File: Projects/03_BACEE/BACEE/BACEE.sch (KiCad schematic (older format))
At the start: 13 parts, among them U1 DS1337_MLv1, U2 24LC1025, U3 24LC1025, U4 ATmega328P-AU, Y1 Crystal 32MHz, Y2 Crystal 16MHz

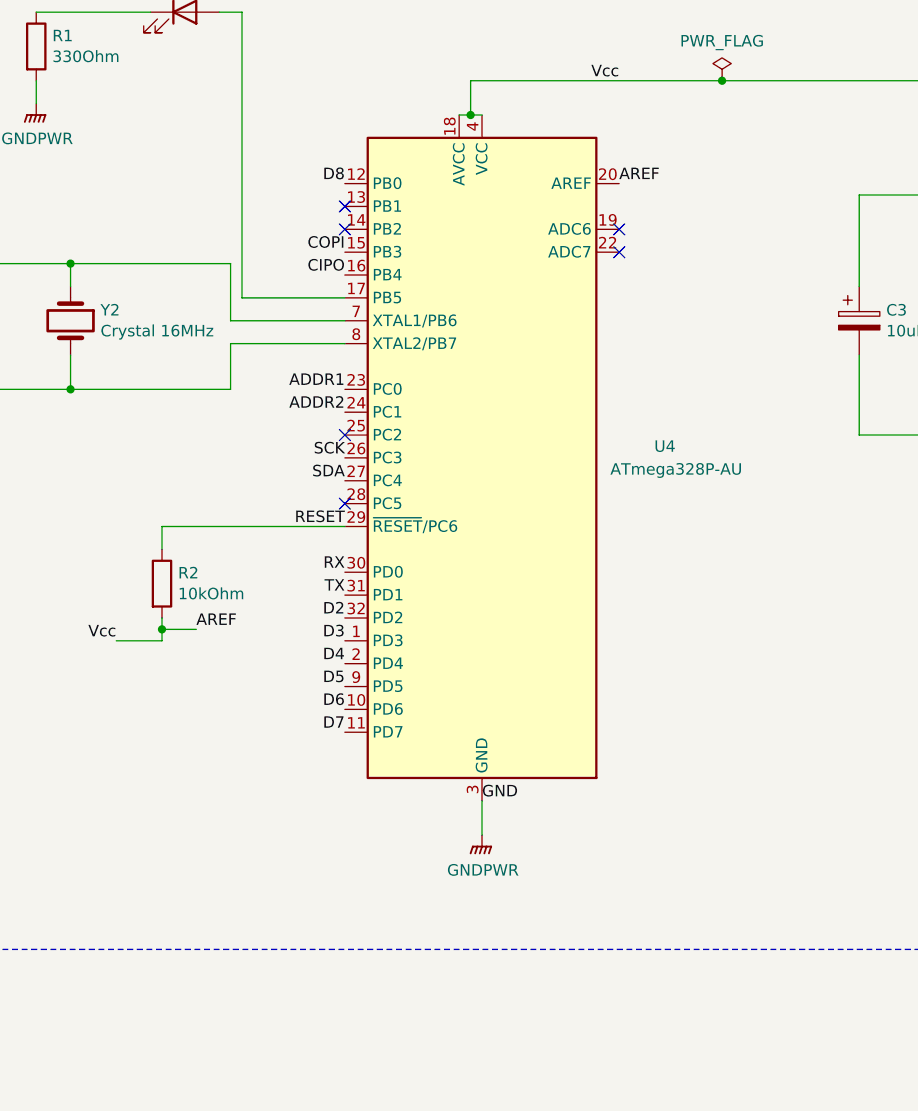
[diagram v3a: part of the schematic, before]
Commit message: Project 3: Edit schematic by changing AREF to Vcc
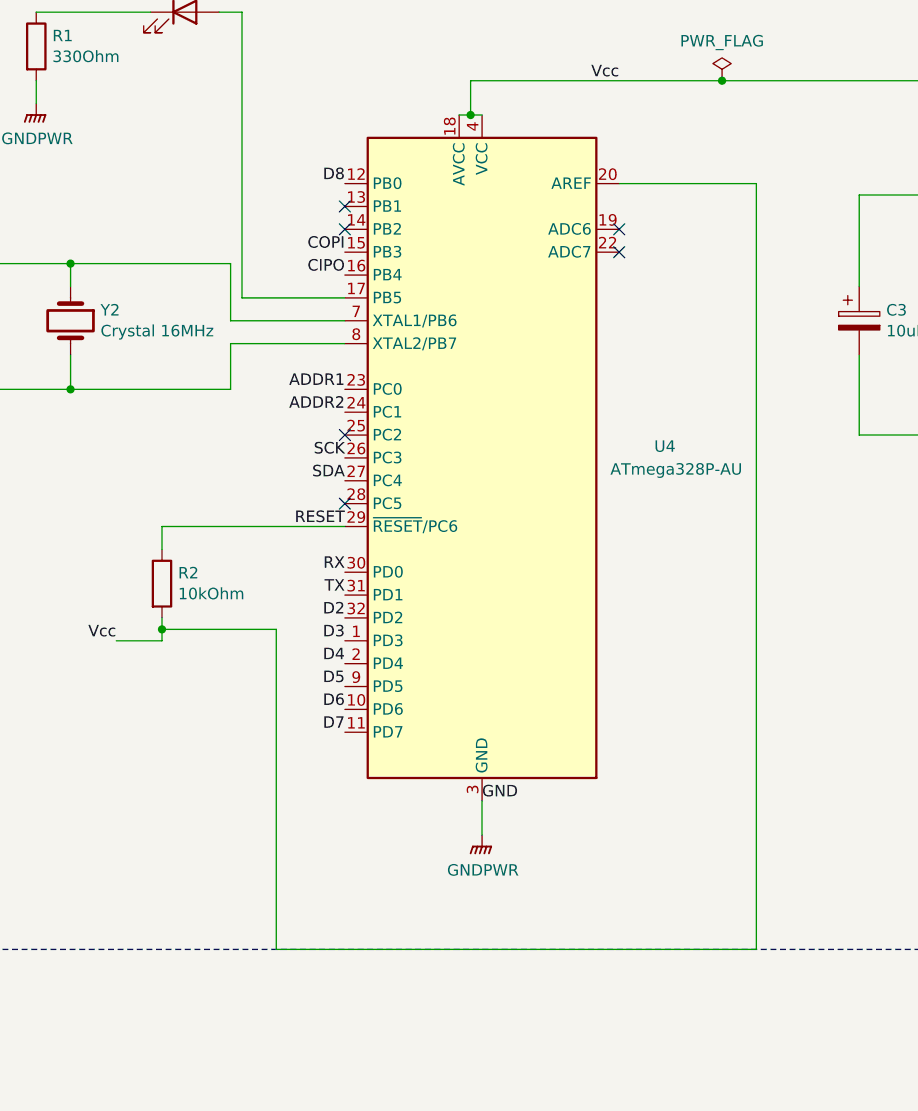
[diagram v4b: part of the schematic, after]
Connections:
- net AREF renamed Vcc
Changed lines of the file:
@@
 Wire Wire Line
 	6150 3850 6150 3750
-Wire Wire Line
-	6150 4150 6150 4200
-Text Label 8150 2250 0    50   ~ 0
-AREF
-Text Label 6300 4200 0    50   ~ 0
-AREF
-Wire Wire Line
-	6300 4200 6150 4200
-Connection ~ 6150 4200
-Wire Wire Line
-	6150 4200 6150 4250
 $Comp
 L power:GNDPWR #PWR0107
@@
 Text Notes 800  5050 0    50   ~ 0
 N4 - Connectors
+Wire Wire Line
+	6150 4150 6150 4200
+Wire Wire Line
+	6150 4200 6650 4200
+Wire Wire Line
+	6650 4200 6650 5600
+Wire Wire Line
+	6650 5600 8750 5600
+Wire Wire Line
+	8750 5600 8750 2250
+Wire Wire Line
+	8750 2250 8150 2250
+Connection ~ 6150 4200
+Wire Wire Line
+	6150 4200 6150 4250
 $EndSCHEMATC
